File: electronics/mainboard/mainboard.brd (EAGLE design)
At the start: 100 x 80 mm, 60 parts, among them CON1 B3B-ZR, IC1 TPS6300, IC2 TPS77033, J1 2MMPAD, J10 2MMPAD, J2 2MMPAD, J3 2MMPAD, J4 2MMPAD, J5 2MMPAD, J6 2MMPAD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

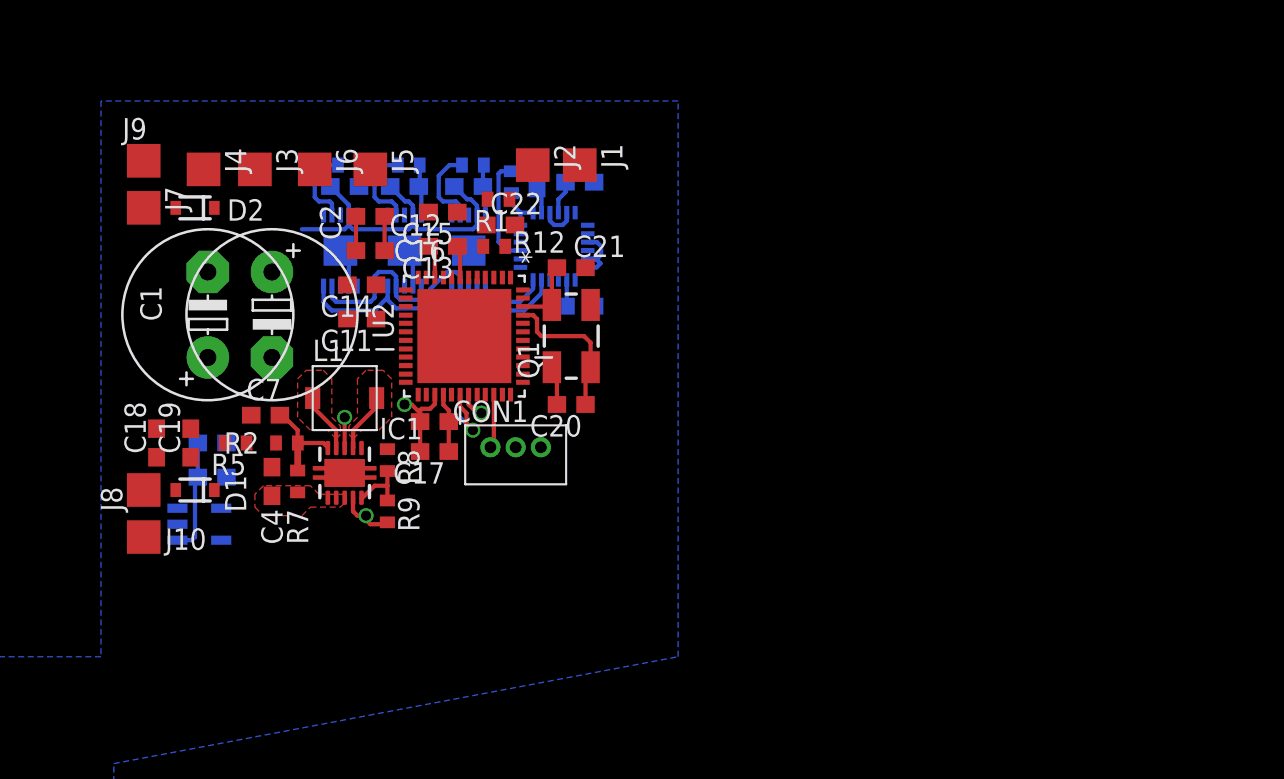
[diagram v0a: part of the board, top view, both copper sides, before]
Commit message: renamed some files and cleaned up.  Added motordriver component
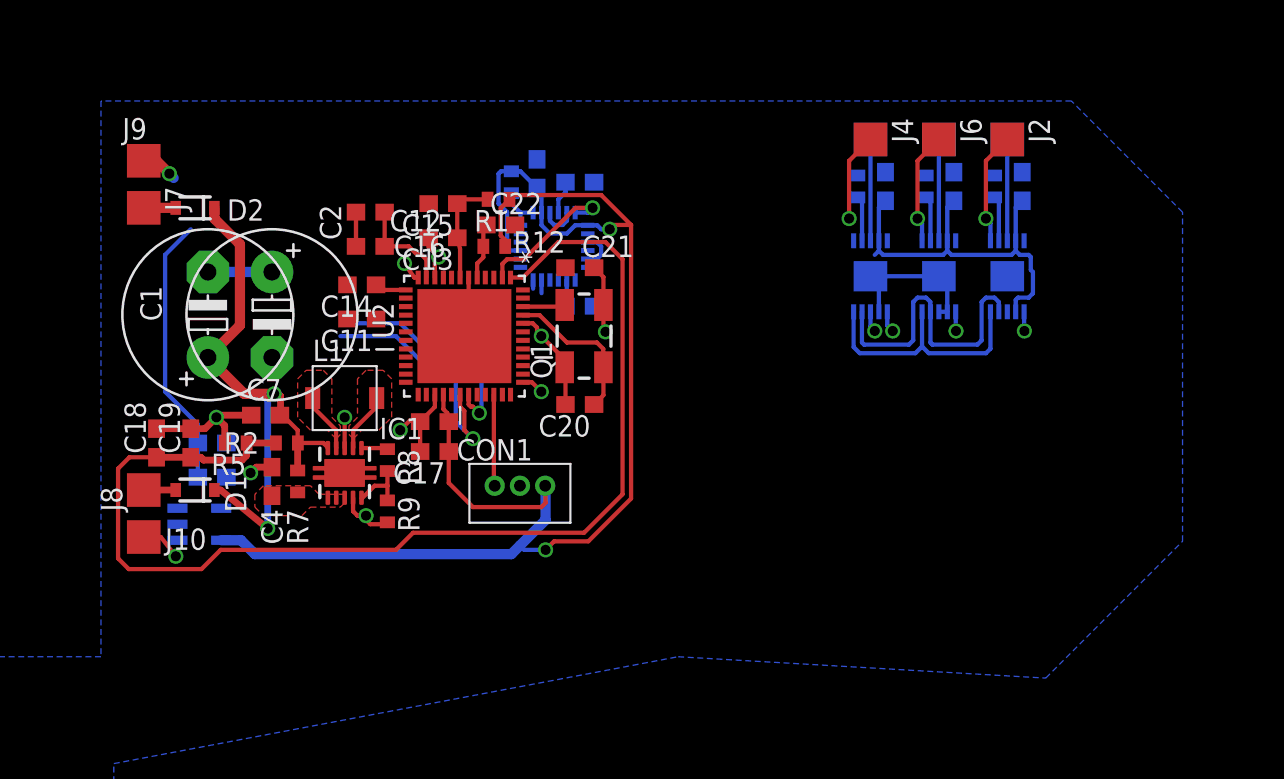
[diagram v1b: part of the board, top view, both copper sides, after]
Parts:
- moved J4 39.7 mm to (63.5, 51.1)
- moved J6 37.1 mm to (67.6, 51.1)
- moved J3 36.6 mm to (63.5, 51.1), flipped to the bottom
- moved J5 33.8 mm to (67.6, 51.1), flipped to the bottom
- moved C6 32.9 mm to (72.5, 48.3), turned to 90 degrees
- moved C5 32.6 mm to (68.5, 48.3), turned to 90 degrees
- moved C3 32.1 mm to (64.4, 48.3), turned to 90 degrees
- moved U4 32.0 mm to (71.6, 42.9)
- moved U3 31.8 mm to (67.6, 42.9)
- moved U1 31.5 mm to (63.5, 42.9)
- moved R10 31.0 mm to (70.9, 48.3), turned to 270 degrees
- moved R11 30.8 mm to (66.8, 48.3), turned to 270 degrees
- moved R6 30.3 mm to (62.7, 48.3), turned to 270 degrees
- moved J2 28.2 mm to (71.6, 51.1)
- moved J1 25.4 mm to (71.6, 51.1), flipped to the bottom
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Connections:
- net IMU_INT: now also U2.2; no longer U2.17
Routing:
- net +3V3: track 15.5 -> 93.6 mm, vias 0 -> 2
- net VSUPP_FEEDBACK: track 0.00 -> 69.9 mm
- net N$2: track 5.90 -> 34.8 mm, vias 0 -> 2
- net GND: track 36.4 -> 62.6 mm, vias 3 -> 12
- net +5V: track 27.7 -> 44.0 mm, vias 0 -> 1
- net SYS_SDA: track 22.3 -> 33.8 mm
- net IMU_INT: track 0.00 -> 8.70 mm, vias 0 -> 1
- net SYS_SCL: track 21.0 -> 29.0 mm
- net N$14: track 0.00 -> 6.66 mm, vias 0 -> 1
- net N$10: track 0.00 -> 6.66 mm, vias 0 -> 1
- net N$6: track 0.00 -> 6.02 mm
- net N$13: track 0.00 -> 6.02 mm
- net N$11: track 0.00 -> 6.02 mm
- net N$12: track 0.00 -> 5.23 mm, vias 0 -> 1
- net N$5: track 1.92 -> 6.32 mm
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
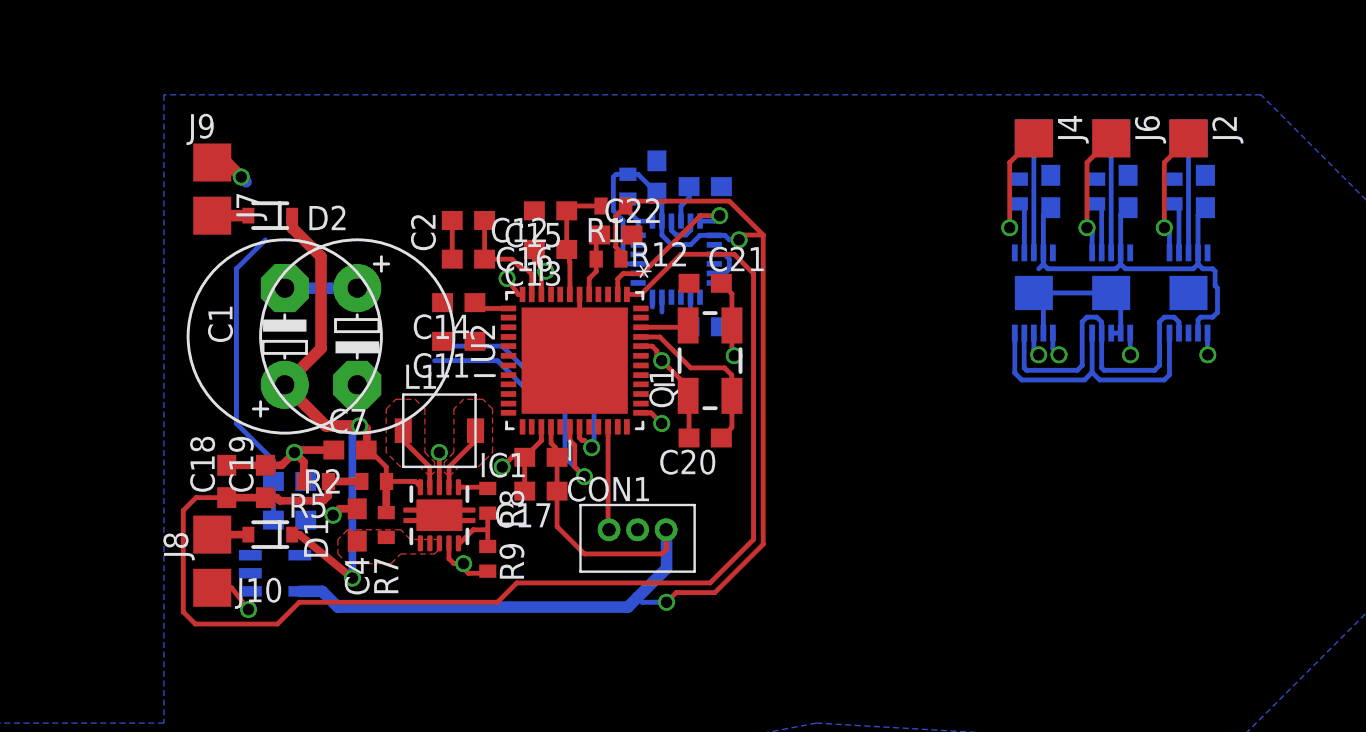
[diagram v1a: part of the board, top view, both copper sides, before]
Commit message: layout mostly done, need to add programming header
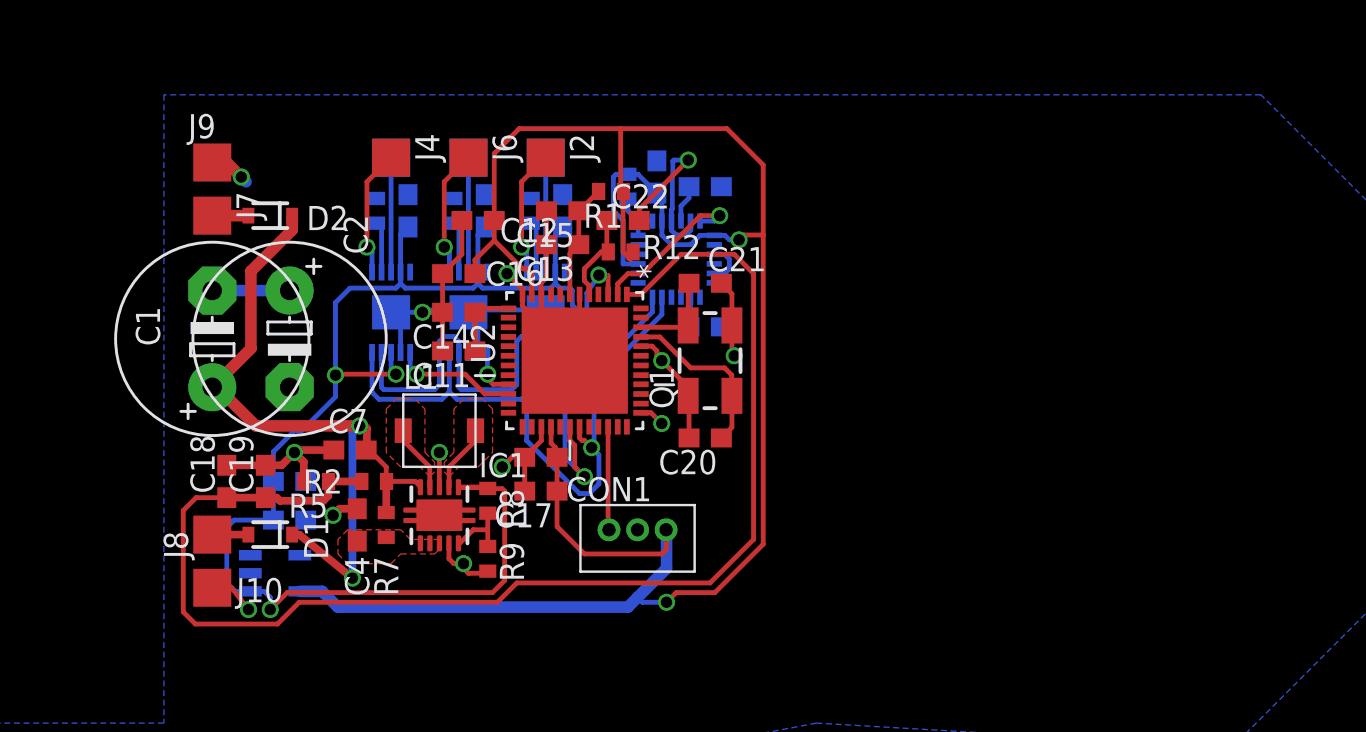
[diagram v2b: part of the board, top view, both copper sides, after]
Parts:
- moved C5 33.8 mm to (34.7, 47.2)
- moved J1 33.8 mm to (37.8, 50.0)
- moved J2 33.8 mm to (37.8, 50.0)
- moved R11 33.8 mm to (33.0, 47.2)
- moved U4 33.8 mm to (37.8, 41.9)
- moved C3 33.8 mm to (30.6, 47.2)
- moved C6 33.8 mm to (38.7, 47.2)
- moved J3 33.8 mm to (29.7, 50.0)
- moved J4 33.8 mm to (29.7, 50.0)
- moved J5 33.8 mm to (33.8, 50.0)
- moved J6 33.8 mm to (33.8, 50.0)
- moved R10 33.8 mm to (37.1, 47.2)
- moved R6 33.8 mm to (29.0, 47.2)
- moved U1 33.8 mm to (29.7, 41.9)
- moved U3 33.8 mm to (33.8, 41.9)
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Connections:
- net DRIVER_FAULT_1: now also U2.21; no longer U2.14
- net DRIVER_FAULT_2: now also U2.3; no longer U2.15
- net DRIVER_FAULT_3: now also U2.22; no longer U2.16
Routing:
- net +5V: track 44.0 -> 78.2 mm, vias 1 -> 3
- net GND: track 62.6 -> 90.9 mm, vias 12 -> 13
- net +3V3: track 93.6 -> 113.7 mm
- net SYS_SCL: track 29.0 -> 36.1 mm
- net DRIVER_FAULT_3: track 1.27 -> 6.56 mm
- net DRIVER_FAULT_2: track 1.15 -> 6.33 mm
- net N$2: track 34.8 -> 39.0 mm
- net SYS_SDA: track 33.8 -> 37.9 mm
- net N$16: track 2.52 -> 4.76 mm
- net N$20: track 3.35 -> 5.35 mm
- net N$7: track 1.89 -> 3.86 mm
- net DRIVER_FAULT_1: track 1.15 -> 2.61 mm
- net N$12: track 5.23 -> 6.66 mm

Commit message: prelim finished board
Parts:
- added J11, J12, J13, J14, J15, J16: ROUND1MM, connectors:ROUND1MM
- added R14: 47k, rcl:R0402
- moved C17 3.33 mm to (40.8, 31.5), turned to 270 degrees
- moved CON1 2.70 mm to (44.7, 32.3)
- moved C10 2.56 mm to (38.7, 32.0), turned to 270 degrees
- moved R1 0.52 mm to (41.8, 48.4)
- moved C15 0.25 mm to (38.7, 47.5)
- moved C20 0.13 mm to (46.2, 35.4)
- moved C21 0.13 mm to (46.2, 43.3)
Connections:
- new net N$24: J11.P$1, U2.23
- new net N$25: J12.P$1, U2.24
- new net N$26: J13.P$1, U2.25
- new net N$27: J14.P$1, U2.26
- new net N$28: J16.P$1, U2.47
- new net RESET: J15.P$1, R14.2, U2.48
- net +3V3: now also R14.1
- net GND: now also U2.41
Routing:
- net N$24: track 0.00 -> 10.1 mm
- net N$27: track 0.00 -> 9.78 mm
- net N$25: track 0.00 -> 9.27 mm
- net N$26: track 0.00 -> 9.03 mm
- net SAT_SERIAL: track 5.43 -> 0.00 mm
- net RESET: track 0.00 -> 4.94 mm
- net +3V3: track 113.7 -> 110.1 mm, vias 2 -> 3
- net GND: track 90.9 -> 93.6 mm
- net VSUPP_FEEDBACK: track 69.9 -> 72.2 mm
- net N$5: track 6.05 -> 7.46 mm
- net N$28: track 0.00 -> 1.21 mm
- net SYS_SDA: track 37.9 -> 37.1 mm
- removed copper zone on layer 16, net GND

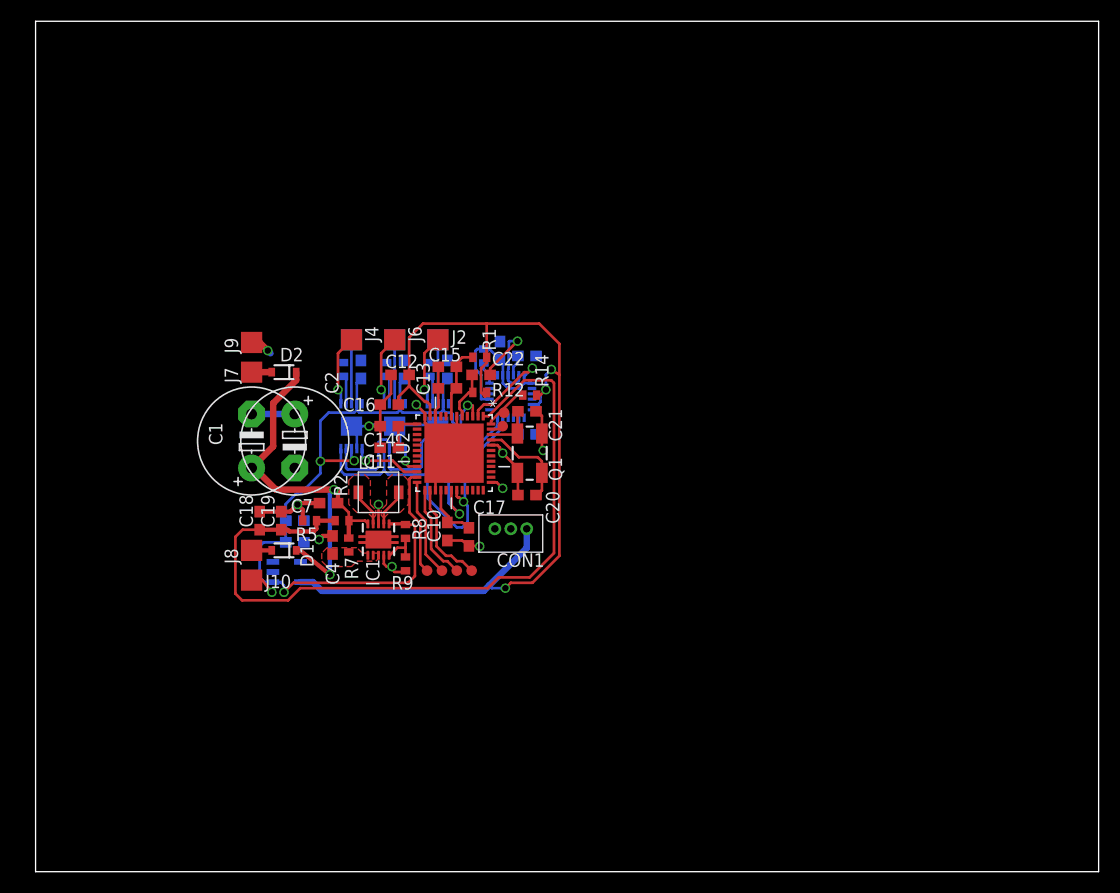
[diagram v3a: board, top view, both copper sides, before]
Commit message: changed crystal.  name change.  minor tweaks
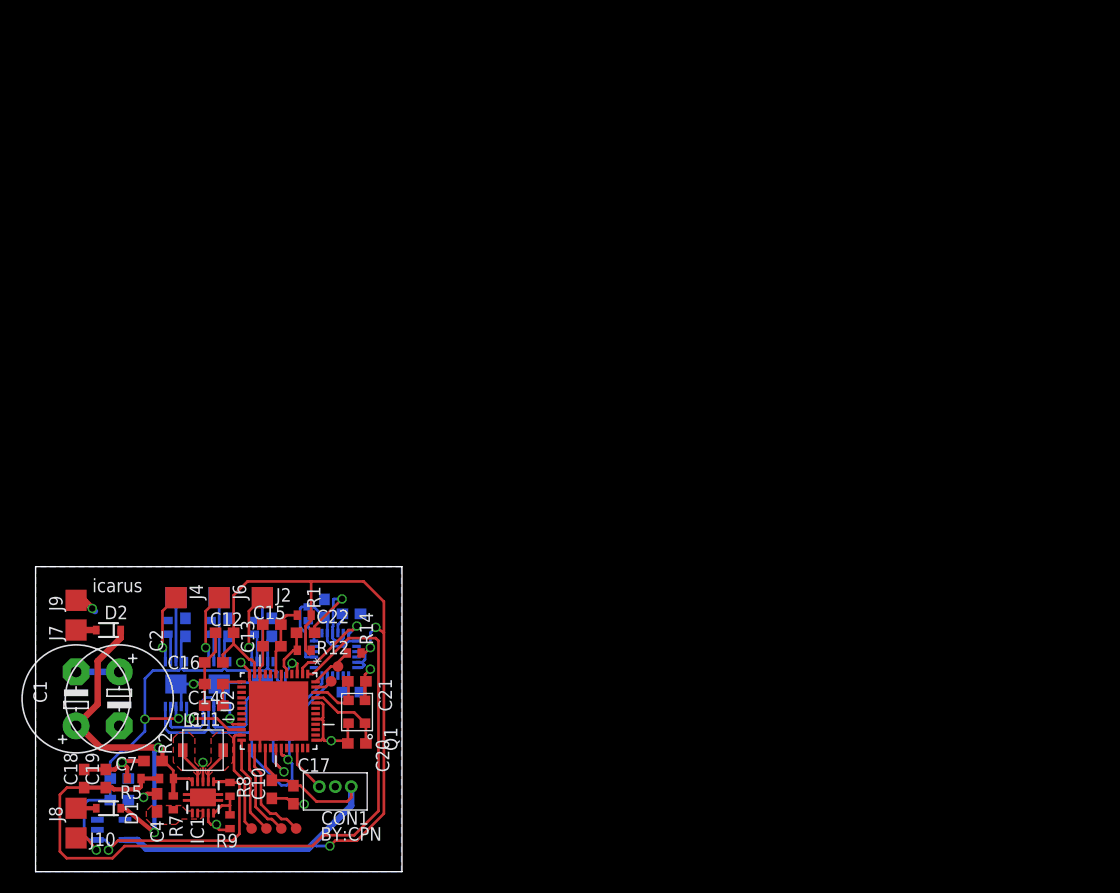
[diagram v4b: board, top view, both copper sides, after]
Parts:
- Q1: device SparkFun-FreqCtrl:CRYSTAL-SMD-5X3 -> crystals:SMD-3.2X2.5
- moved C21 30.0 mm to (30.2, 17.9)
- moved Q1 29.8 mm to (31.0, 14.0)
- moved C18 29.3 mm to (4.57, 8.76)
- moved C19 29.3 mm to (6.60, 8.76)
- moved C25 29.3 mm to (29.7, 16.9)
- moved C9 29.3 mm to (7.87, 8.76)
- moved CON1 29.3 mm to (28.2, 8.00)
- moved C16 29.3 mm to (16.8, 19.7)
- moved C24 29.3 mm to (29.7, 24.3)
- moved C4 29.3 mm to (11.4, 6.48)
- moved IC1 29.3 mm to (15.7, 6.99)
- moved J13 29.3 mm to (23.1, 4.06)
- moved J14 29.3 mm to (24.5, 4.06)
- moved J7 29.3 mm to (3.81, 22.7)
- moved R1 29.3 mm to (25.3, 24.1)
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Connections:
- net GND: now also Q1.P$2, Q1.P$4; no longer Q1.2, Q1.4
- net N$15: now also Q1.P$1; no longer Q1.1
- net N$16: now also Q1.P$3; no longer Q1.3
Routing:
- net +3V3: track 110.1 -> 117.3 mm
- net SAT_SERIAL: track 0.00 -> 4.49 mm
- net GND: track 93.6 -> 96.6 mm, vias 13 -> 12
- net N$15: track 9.06 -> 7.58 mm
- net N$16: track 4.78 -> 5.42 mm
- net RESET: track 4.94 -> 4.34 mm
- added copper zone on layer 16, net GND
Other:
- board size 100 x 80 mm -> 34.5 x 28.7 mm
- board text added: "BY:CPN"
- board text added: "icarus"

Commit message: minor changes for board production.  REV0 off to board house
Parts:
- added J17, J18, J19, J20: ROUND1MM, connectors:ROUND1MM
- moved CON1 2.65 mm to (29.0, 5.46)
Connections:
- new net N$29: J17.P$1, U2.36
- new net N$30: J18.P$1, U2.35
- new net N$31: J19.P$1, U2.38
- new net N$32: J20.P$1, U2.40
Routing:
- net N$32: track 0.00 -> 7.72 mm
- net N$31: track 0.00 -> 6.37 mm
- net N$29: track 0.00 -> 3.63 mm
- net SAT_SERIAL: track 4.49 -> 7.35 mm
- net N$30: track 0.00 -> 2.31 mm
- net GND: track 96.6 -> 95.6 mm, vias 12 -> 14
- net +3V3: track 117.3 -> 116.8 mm
